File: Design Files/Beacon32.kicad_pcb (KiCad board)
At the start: 2 copper layers, 46.1 x 46.1 mm, 39 parts, among them M1 ESP-WROOM-32, P1 CONN_01X01, P10 CONN_01X01, P11 CONN_01X01, P12 CONN_01X01, P13 CONN_01X01, P14 CONN_01X01, P15 CONN_01X01, P16 CONN_01X01, P17 CONN_01X02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

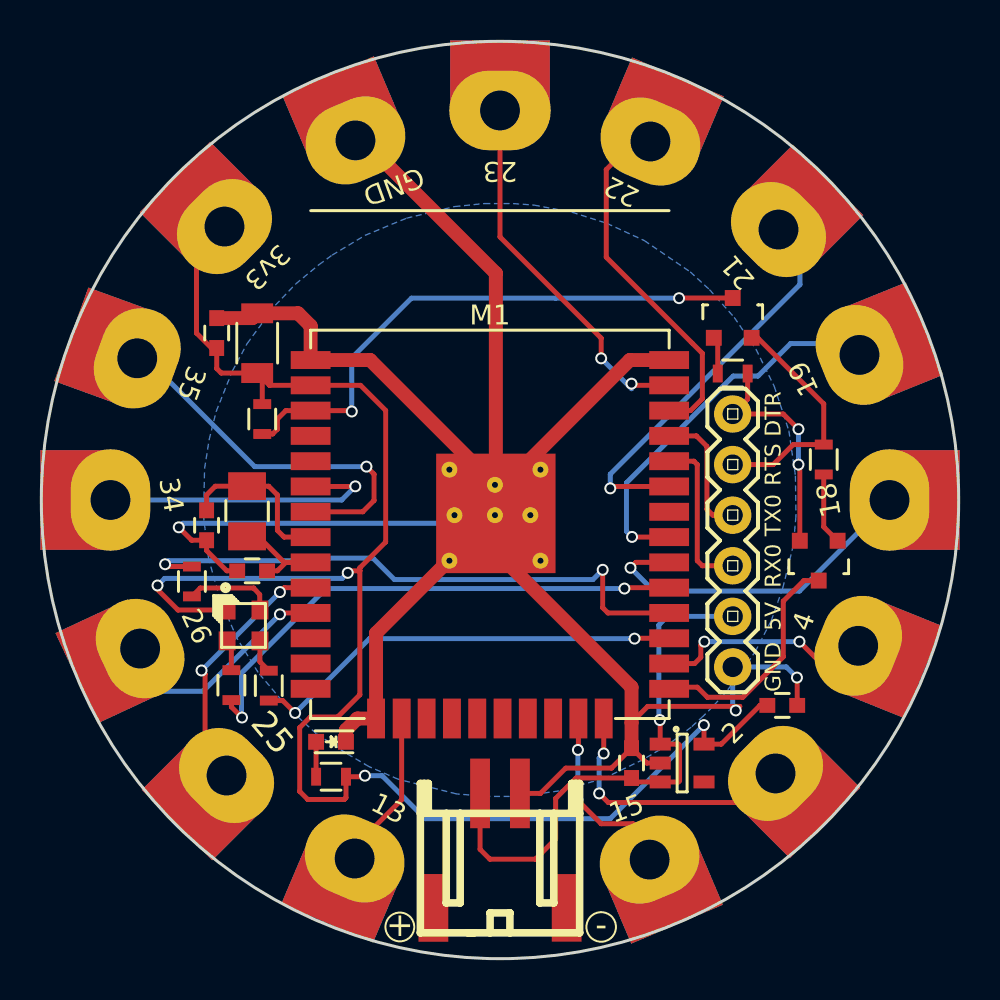
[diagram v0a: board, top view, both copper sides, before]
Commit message: Issue closed
Added Reset switch and RGB footprint changed
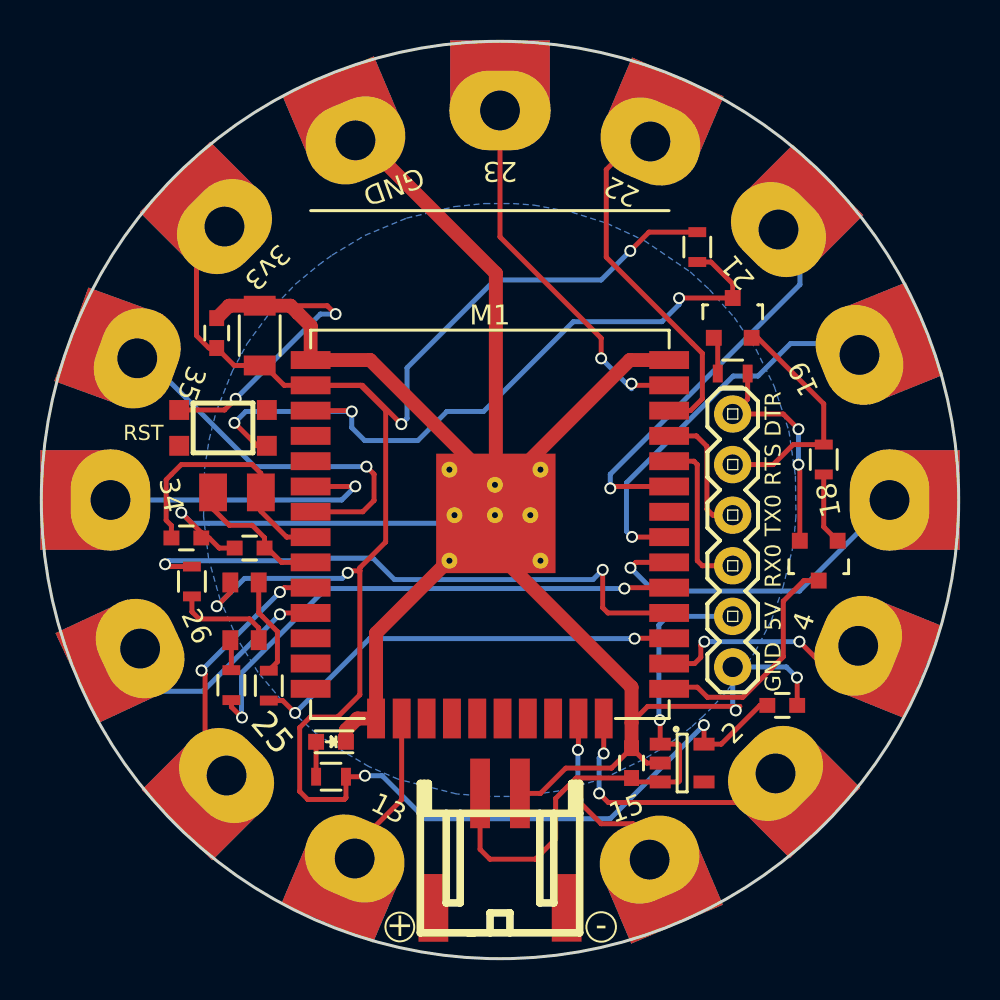
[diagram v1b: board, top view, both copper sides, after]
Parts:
- added SW1: SW_PUSH, Explore:smd_push2_New, F.Cu at (70.4, 140.9)
- R1: value 10K -> 10k
- U3: footprint EE:Logo_8 -> Logo:Logo_8
- U7: footprint RGB LED:sfh5712 -> Explore:RGB_SMD_4pin_New
- Y1: footprint EE:SMD_RTC_Crstl -> Explore:SMD_RTC_Crstl
- moved R1 23.5 mm to (94.2, 131.8)
- moved C3 1.20 mm to (68.6, 146.4), turned to 0 degrees
- moved C4 1.15 mm to (71.8, 146.9)
- moved Y1 1.02 mm to (71.1, 144.1), turned to 180 degrees
- moved U7 0.71 mm to (71.5, 150.1)
- moved C1 0.40 mm to (72.3, 136.3)
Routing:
- net +3V3: track 86.0 -> 104.2 mm, vias 4 -> 6
- net GND: track 126.1 -> 139.7 mm, vias 3 -> 5
- net /EN: track 28.4 -> 36.8 mm, vias 2 -> 3
- net Net-(C3-Pad1): track 8.97 -> 13.2 mm
- net Net-(R9-Pad2): track 1.68 -> 5.00 mm
- net Net-(C4-Pad1): track 6.18 -> 7.26 mm
- net Net-(R8-Pad2): track 4.51 -> 5.08 mm
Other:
- board text added: "RST"
- board text added: "v0.2"
- board text removed: "v0.1"

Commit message: Drill Size Increased
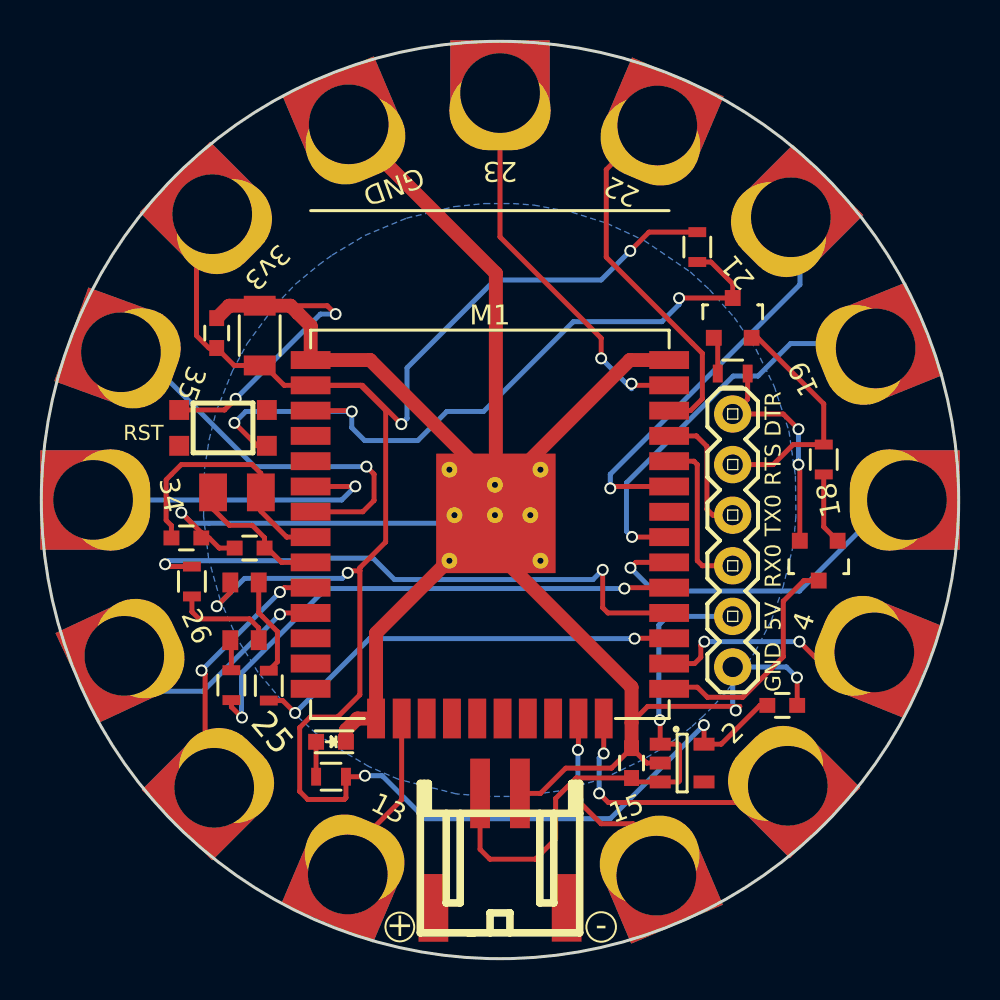
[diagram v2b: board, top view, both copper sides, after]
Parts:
- P1, P10, P11, P12, P13, P14, P15, P16, P3, P4, P5, P6, P7, P8, P9: footprint Special pad:Specialpad -> pad:MinimaPad

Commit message: Resized pads to 3.5mm
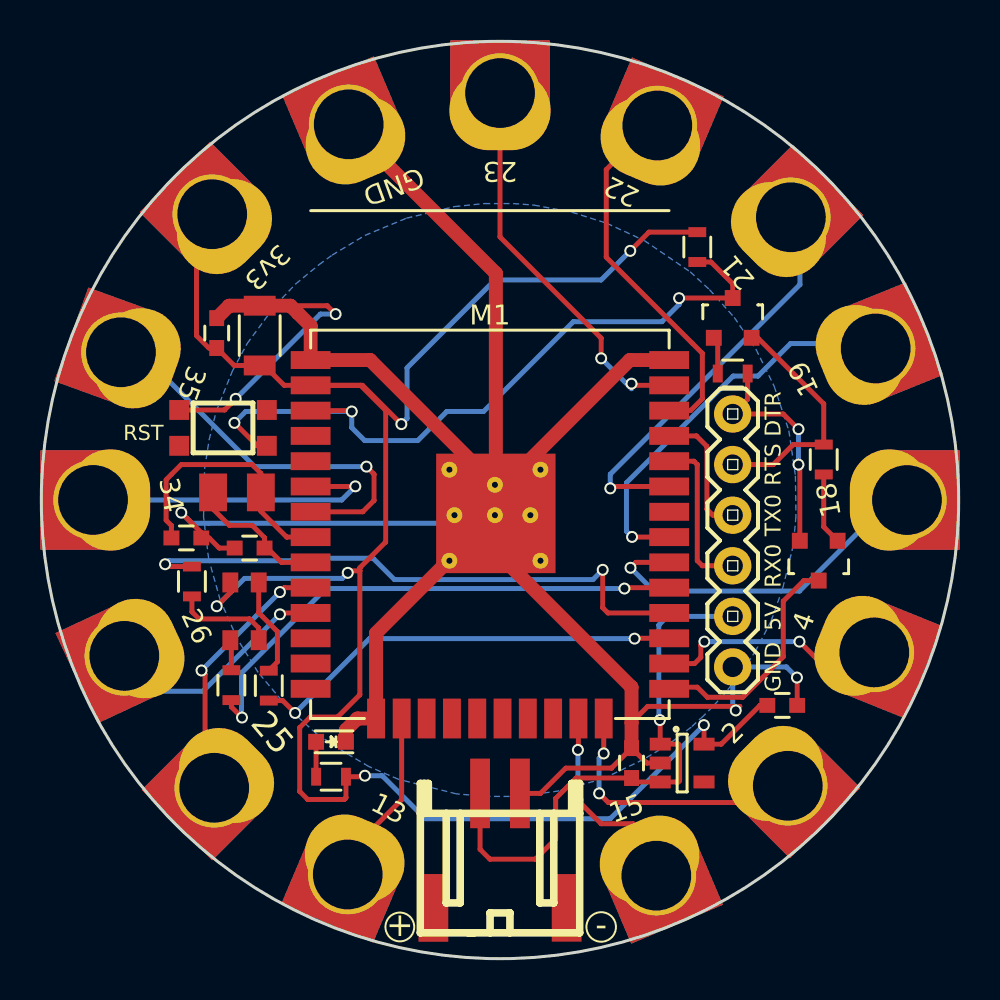
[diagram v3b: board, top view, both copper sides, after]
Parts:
- P1, P10, P11, P12, P13, P14, P15, P16, P3, P4, P5, P6, P7, P8, P9: footprint pad:MinimaPad -> pad:MinimaPad_3.5mm
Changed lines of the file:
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@@
       (net 19 "Net-(C4-Pad1)"))
   )
-  (module pad:MinimaPad (layer F.Cu)
+  (module pad:MinimaPad_3.5mm (layer F.Cu)
     (at 69.596 129.54 225)
     (descr "module 1 pin (ou trou mecanique de percage)")
@@
     (pad 1 smd trapezoid (at 0.254 0 225) (size 5 4) (layers *.Mask B.Cu F.Paste)
       (net 2 +3V3))
-    (pad 2 thru_hole circle (at 0.25 -0.65 315) (size 4 4) (drill 4) (layers *.Cu *.Mask))
-  )
-  (module pad:MinimaPad (layer F.Cu)
+    (pad 2 thru_hole circle (at 0.25 -0.65 315) (size 4 4) (drill 3.5) (layers *.Cu *.Mask))
+  )
+  (module pad:MinimaPad_3.5mm (layer F.Cu)
     (at 99.568 130.048 135)
     (descr "module 1 pin (ou trou mecanique de percage)")
@@
     (pad 1 smd trapezoid (at 0.254 0 135) (size 5 4) (layers *.Mask B.Cu F.Paste)
       (net 43 /21))
-    (pad 2 thru_hole circle (at 0.25 -0.65 225) (size 4 4) (drill 4) (layers *.Cu *.Mask))
-  )
-  (module pad:MinimaPad (layer F.Cu)
+    (pad 2 thru_hole circle (at 0.25 -0.65 225) (size 4 4) (drill 3.5) (layers *.Cu *.Mask))
+  )
+  (module pad:MinimaPad_3.5mm (layer F.Cu)
     (at 92.71 125.222 157)
     (descr "module 1 pin (ou trou mecanique de percage)")
@@
     (pad 1 smd trapezoid (at 0.254 0 157) (size 5 4) (layers *.Mask B.Cu F.Paste)
       (net 44 /22))
-    (pad 2 thru_hole circle (at 0.25 -0.65 247) (size 4 4) (drill 4) (layers *.Cu *.Mask))
-  )
-  (module pad:MinimaPad (layer F.Cu)
+    (pad 2 thru_hole circle (at 0.25 -0.65 247) (size 4 4) (drill 3.5) (layers *.Cu *.Mask))
+  )
+  (module pad:MinimaPad_3.5mm (layer F.Cu)
     (at 99.06 159.512 45)
     (descr "module 1 pin (ou trou mecanique de percage)")
@@
     (pad 1 smd trapezoid (at 0.254 0 45) (size 5 4) (layers *.Mask B.Cu F.Paste)
       (net 23 /2))
-    (pad 2 thru_hole circle (at 0.25 -0.65 135) (size 4 4) (drill 4) (layers *.Cu *.Mask))
-  )
-  (module pad:MinimaPad (layer F.Cu)
+    (pad 2 thru_hole circle (at 0.25 -0.65 135) (size 4 4) (drill 3.5) (layers *.Cu *.Mask))
+  )
+  (module pad:MinimaPad_3.5mm (layer F.Cu)
     (at 84.582 123.444 180)
     (descr "module 1 pin (ou trou mecanique de percage)")
@@
     (pad 1 smd trapezoid (at 0.254 0 180) (size 5 4) (layers *.Mask B.Cu F.Paste)
       (net 45 /23))
-    (pad 2 thru_hole circle (at 0.25 -0.65 270) (size 4 4) (drill 4) (layers *.Cu *.Mask))
-  )
-  (module pad:MinimaPad (layer F.Cu)
+    (pad 2 thru_hole circle (at 0.25 -0.65 270) (size 4 4) (drill 3.5) (layers *.Cu *.Mask))
+  )
+  (module pad:MinimaPad_3.5mm (layer F.Cu)
     (at 103.886 136.906 112)
     (descr "module 1 pin (ou trou mecanique de percage)")
@@
     (pad 1 smd trapezoid (at 0.254 0 112) (size 5 4) (layers *.Mask B.Cu F.Paste)
       (net 42 /19))
-    (pad 2 thru_hole circle (at 0.25 -0.65 202) (size 4 4) (drill 4) (layers *.Cu *.Mask))
-  )
-  (module pad:MinimaPad (layer F.Cu)
+    (pad 2 thru_hole circle (at 0.25 -0.65 202) (size 4 4) (drill 3.5) (layers *.Cu *.Mask))
+  )
+  (module pad:MinimaPad_3.5mm (layer F.Cu)
     (at 105.41 144.78 90)
     (descr "module 1 pin (ou trou mecanique de percage)")
@@
     (pad 1 smd trapezoid (at 0.254 0 90) (size 5 4) (layers *.Mask B.Cu F.Paste)
       (net 41 /18))
-    (pad 2 thru_hole circle (at 0.25 -0.65 180) (size 4 4) (drill 4) (layers *.Cu *.Mask))
-  )
-  (module pad:MinimaPad (layer F.Cu)
+    (pad 2 thru_hole circle (at 0.25 -0.65 180) (size 4 4) (drill 3.5) (layers *.Cu *.Mask))
+  )
+  (module pad:MinimaPad_3.5mm (layer F.Cu)
     (at 63.246 144.272 270)
     (descr "module 1 pin (ou trou mecanique de percage)")
@@
     (pad 1 smd trapezoid (at 0.254 0 270) (size 5 4) (layers *.Mask B.Cu F.Paste)
       (net 34 /34))
-    (pad 2 thru_hole circle (at 0.25 -0.65) (size 4 4) (drill 4) (layers *.Cu *.Mask))
-  )
-  (module pad:MinimaPad (layer F.Cu)
+    (pad 2 thru_hole circle (at 0.25 -0.65) (size 4 4) (drill 3.5) (layers *.Cu *.Mask))
+  )
+  (module pad:MinimaPad_3.5mm (layer F.Cu)
     (at 64.77 136.652 250)
     (descr "module 1 pin (ou trou mecanique de percage)")
@@
     (pad 1 smd trapezoid (at 0.254 0 250) (size 5 4) (layers *.Mask B.Cu F.Paste)
       (net 35 /35))
-    (pad 2 thru_hole circle (at 0.25 -0.65 340) (size 4 4) (drill 4) (layers *.Cu *.Mask))
-  )
-  (module pad:MinimaPad (layer F.Cu)
+    (pad 2 thru_hole circle (at 0.25 -0.65 340) (size 4 4) (drill 3.5) (layers *.Cu *.Mask))
+  )
+  (module pad:MinimaPad_3.5mm (layer F.Cu)
     (at 103.632 152.654 68)
     (descr "module 1 pin (ou trou mecanique de percage)")
@@
     (pad 1 smd trapezoid (at 0.254 0 68) (size 5 4) (layers *.Mask B.Cu F.Paste)
       (net 24 /4))
-    (pad 2 thru_hole circle (at 0.25 -0.65 158) (size 4 4) (drill 4) (layers *.Cu *.Mask))
-  )
-  (module pad:MinimaPad (layer F.Cu)
+    (pad 2 thru_hole circle (at 0.25 -0.65 158) (size 4 4) (drill 3.5) (layers *.Cu *.Mask))
+  )
+  (module pad:MinimaPad_3.5mm (layer F.Cu)
     (at 92.202 164.084 23)
     (descr "module 1 pin (ou trou mecanique de percage)")
@@
     (pad 1 smd trapezoid (at 0.254 0 23) (size 5 4) (layers *.Mask B.Cu F.Paste)
       (net 46 /15))
-    (pad 2 thru_hole circle (at 0.25 -0.65 113) (size 4 4) (drill 4) (layers *.Cu *.Mask))
-  )
-  (module pad:MinimaPad (layer F.Cu)
+    (pad 2 thru_hole circle (at 0.25 -0.65 113) (size 4 4) (drill 3.5) (layers *.Cu *.Mask))
+  )
+  (module pad:MinimaPad_3.5mm (layer F.Cu)
     (at 76.2 163.83 337)
     (descr "module 1 pin (ou trou mecanique de percage)")
@@
     (pad 1 smd trapezoid (at 0.254 0 337) (size 5 4) (layers *.Mask B.Cu F.Paste)
       (net 22 /13))
-    (pad 2 thru_hole circle (at 0.25 -0.65 67) (size 4 4) (drill 4) (layers *.Cu *.Mask))
-  )
-  (module pad:MinimaPad (layer F.Cu)
+    (pad 2 thru_hole circle (at 0.25 -0.65 67) (size 4 4) (drill 3.5) (layers *.Cu *.Mask))
+  )
+  (module pad:MinimaPad_3.5mm (layer F.Cu)
     (at 69.342 159.258 315)
     (descr "module 1 pin (ou trou mecanique de percage)")
@@
     (pad 1 smd trapezoid (at 0.254 0 315) (size 5 4) (layers *.Mask B.Cu F.Paste)
       (net 36 /25))
-    (pad 2 thru_hole circle (at 0.25 -0.65 45) (size 4 4) (drill 4) (layers *.Cu *.Mask))
-  )
-  (module pad:MinimaPad (layer F.Cu)
+    (pad 2 thru_hole circle (at 0.25 -0.65 45) (size 4 4) (drill 3.5) (layers *.Cu *.Mask))
+  )
+  (module pad:MinimaPad_3.5mm (layer F.Cu)
     (at 64.77 152.4 295)
     (descr "module 1 pin (ou trou mecanique de percage)")
@@
     (pad 1 smd trapezoid (at 0.254 0 295) (size 5 4) (layers *.Mask B.Cu F.Paste)
       (net 37 /26))
-    (pad 2 thru_hole circle (at 0.25 -0.65 25) (size 4 4) (drill 4) (layers *.Cu *.Mask))
-  )
-  (module pad:MinimaPad (layer F.Cu)
+    (pad 2 thru_hole circle (at 0.25 -0.65 25) (size 4 4) (drill 3.5) (layers *.Cu *.Mask))
+  )
+  (module pad:MinimaPad_3.5mm (layer F.Cu)
     (at 76.708 124.968 203)
     (descr "module 1 pin (ou trou mecanique de percage)")
@@
     (pad 1 smd trapezoid (at 0.254 0 203) (size 5 4) (layers *.Mask B.Cu F.Paste)
       (net 1 GND))
-    (pad 2 thru_hole circle (at 0.25 -0.65 293) (size 4 4) (drill 4) (layers *.Cu *.Mask))
+    (pad 2 thru_hole circle (at 0.25 -0.65 293) (size 4 4) (drill 3.5) (layers *.Cu *.Mask))
   )
   (gr_text RST (at 66.421 141.1605) (layer F.SilkS)
